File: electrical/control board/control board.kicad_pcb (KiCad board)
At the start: 4 copper layers, 139.7 x 139.7 mm, 63 parts, among them J1 analog_extra, J10 Motor_2, J11 Motor_3, J12 Motor_4, J13 Motor_5, J14 Motor_6, J15 Motor_7, J16 Motor_8, J2 Programming_Header, J3 USB_B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

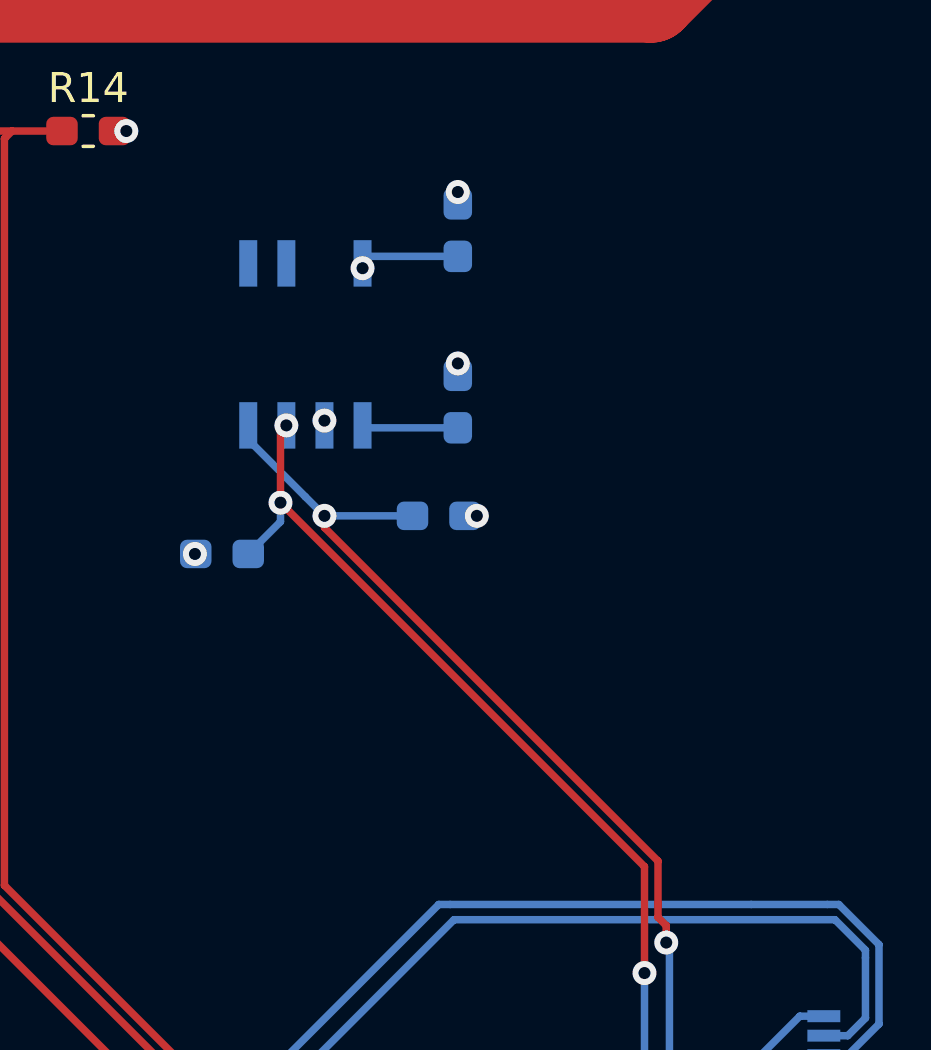
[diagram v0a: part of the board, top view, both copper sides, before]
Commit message: mostly finished routing control board
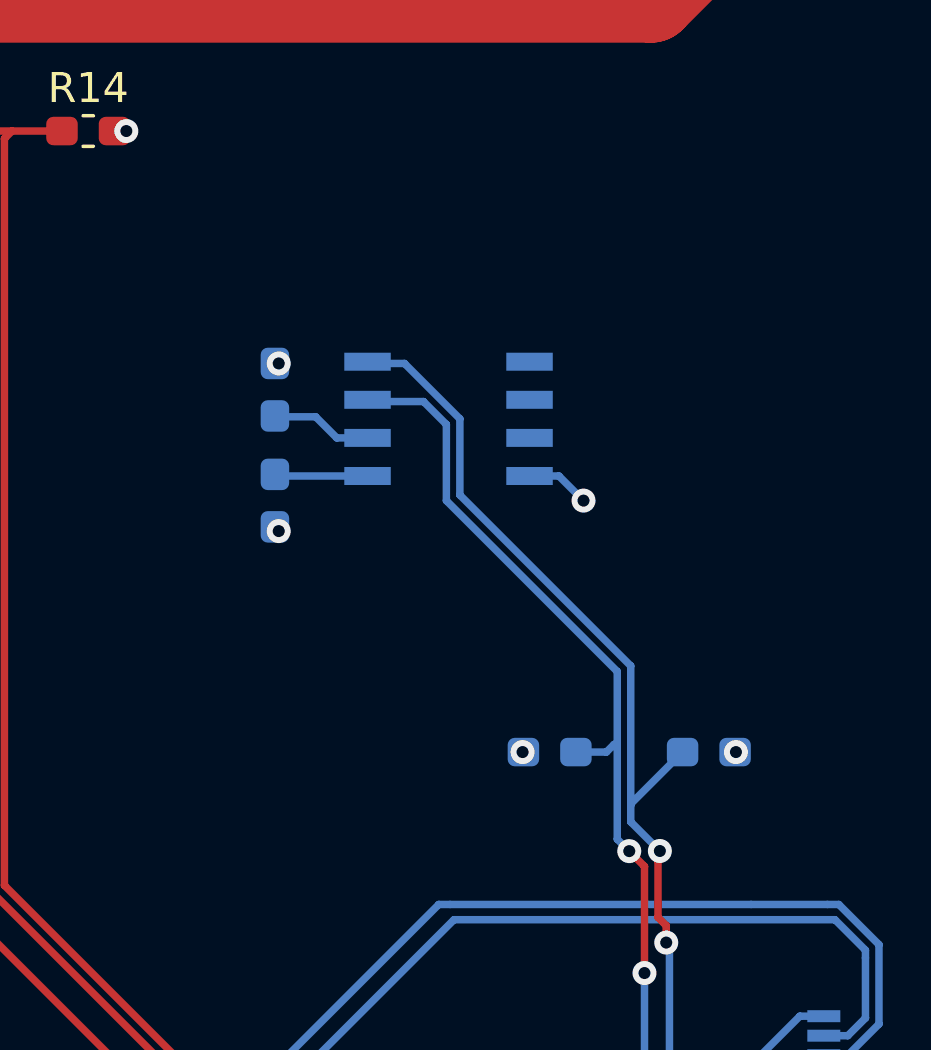
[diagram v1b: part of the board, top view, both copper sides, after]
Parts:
- C1: value 0.1uF -> .22uF
- C4: value 1uF -> .1uF
- R1, R2: value 4.7k -> 2.2k
- U2: value HIH6031 -> HIH6131-021; footprint Package_SO:SOIC-8-N7_3.9x4.9mm_P1.27mm -> Package_SO:SOIC-8_3.9x4.9mm_P1.27mm
- moved R1 12.8 mm to (78.9, 74.7)
- moved R2 12.0 mm to (84.2, 74.7)
- moved C4 10.9 mm to (69.7, 66.3), turned to 270 degrees
- moved C1 6.11 mm to (69.7, 62.6)
- moved U2 5.38 mm to (75.5, 63.6), turned to 0 degrees
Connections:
- C1 pad 2: GND -> +3V3
- C4 pad 1: +3V3 -> Net-(C4-Pad1)
- C4 pad 2: GND -> +3V3
- U2 pad 1: Net-(C1-Pad1) -> Net-(C4-Pad1)
- U2 pad 2: GND -> Net-(C1-Pad1)
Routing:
- net Net-(C4-Pad1): track 0.00 -> 2.98 mm
- net +3V3: track 39.4 -> 38.3 mm, vias 34 -> 36
- net /HIH_SDA: track 62.8 -> 63.5 mm
- net /HIH_SCL: track 60.2 -> 60.0 mm, vias 3 -> 2
- net GND: vias 36 -> 33

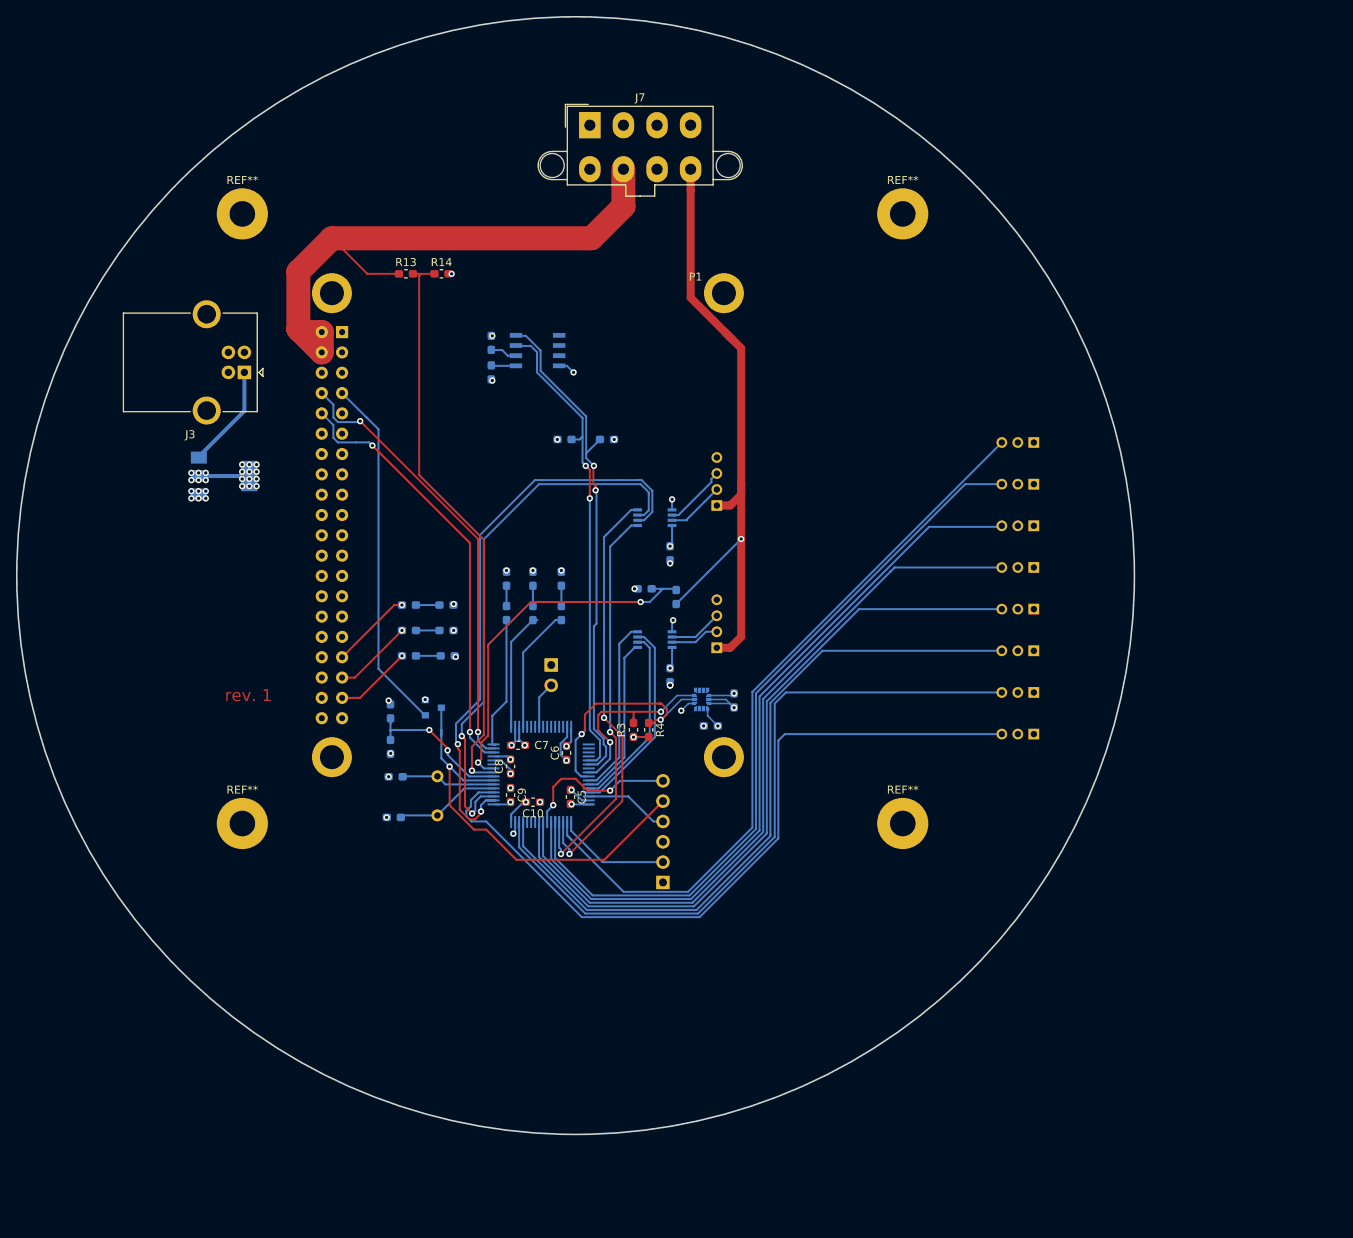
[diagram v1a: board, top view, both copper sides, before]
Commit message: added capacitors to linear regulator
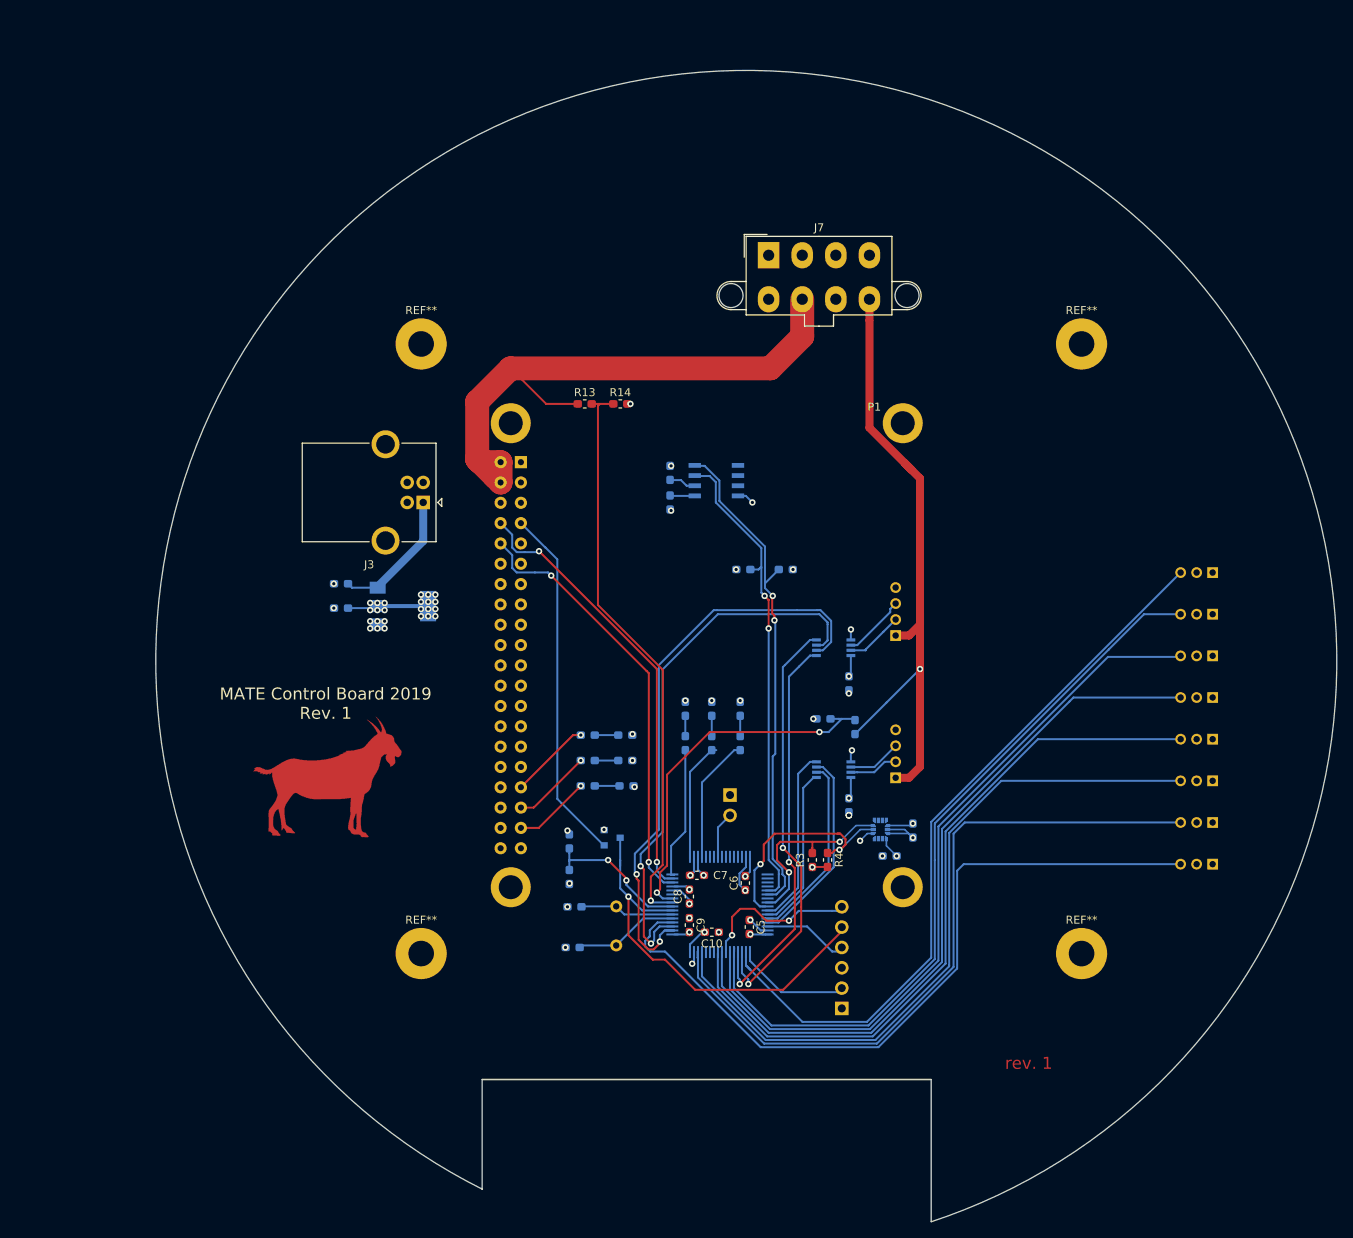
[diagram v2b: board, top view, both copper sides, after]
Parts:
- added C15: 10uF, Capacitor_SMD:C_0603_1608Metric_Pad1.05x0.95mm_HandSolder, B.Cu at (50.9, 92.7)
- added C16: 10uF, Capacitor_SMD:C_0603_1608Metric_Pad1.05x0.95mm_HandSolder, B.Cu at (50.9, 95.8)
- added G***: LOGO, goat:goat_solid_copper_0.731in, F.Cu at (49.3, 116.8)
- moved C8 27.6 mm to (94.5, 131.8)
- moved P1 27.6 mm to (121.2, 72.6)
- moved U2 27.6 mm to (97.9, 79.8)
- moved C11 27.6 mm to (119.5, 126.7)
- moved C12 27.6 mm to (122.4, 123.6)
- moved C13 27.6 mm to (114.4, 120.4)
- moved C14 27.6 mm to (114.4, 105.2)
- moved C3 27.6 mm to (80.1, 133.1)
- moved C4 27.6 mm to (92.1, 82.5)
- moved C9 27.6 mm to (94.5, 135.4)
- moved D1 27.6 mm to (94.0, 108.3)
- moved D4 27.6 mm to (86.5, 111.6)
- moved D5 27.6 mm to (86.5, 114.8)
- moved D6 27.6 mm to (86.6, 118.0)
- moved J1 27.6 mm to (99.6, 119.1)
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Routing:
- net Net-(C15-Pad1): track 13.1 -> 16.8 mm
- net +3V3: track 38.3 -> 41.6 mm
- net GND: vias 33 -> 35
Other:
- board size 139.7 x 139.7 mm -> 147.6 x 143.9 mm
- board text added: "MATE Control Board 2019 Rev. 1"

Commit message: Added pads to access internal layers
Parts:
- added J8: Power_Header, footprints:1x2 individual header, F.Cu at (71.4, 49.8)
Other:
- board text added: "+3.3V"
- board text added: "GND"
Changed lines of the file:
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@@
   (general
     (thickness 1.6)
-    (drawings 6)
+    (drawings 10)
     (tracks 570)
     (zones 0)
-    (modules 66)
+    (modules 67)
     (nets 120)
   )
@@
     )
   )
+  (module "footprints:1x2 individual header" (layer F.Cu)
+    (at 71.374 49.784)
+    (fp_text reference J8 (at 0 0.5) (layer F.SilkS)
+      (effects (font (size 1 1) (thickness 0.15)))
+    )
+    (fp_text value Power_Header (at 0 -0.5) (layer F.Fab)
+      (effects (font (size 1 1) (thickness 0.15)))
+    )
+    (pad 1 thru_hole rect (at -6.35 1.27) (size 1.524 1.524) (drill 0.762) (layers *.Cu *.Mask)
+      (net 1 GND))
+    (pad 2 thru_hole circle (at 6.35 1.27) (size 1.524 1.524) (drill 0.762) (layers *.Cu *.Mask)
+      (net 2 +3V3))
+  )
+  (gr_text +3.3V (at 77.724 48.514) (layer B.SilkS)
+    (effects (font (size 1.5 1.5) (thickness 0.3)) (justify mirror))
+  )
+  (gr_text GND (at 64.77 48.514) (layer B.SilkS)
+    (effects (font (size 1.5 1.5) (thickness 0.3)) (justify mirror))
+  )
+  (gr_text +3.3V (at 77.216 53.594) (layer F.SilkS)
+    (effects (font (size 1.5 1.5) (thickness 0.3)))
+  )
+  (gr_text GND (at 64.77 53.594) (layer F.SilkS)
+    (effects (font (size 1.5 1.5) (thickness 0.3)))
+  )
   (gr_text "MATE Control Board 2019\nRev. 1" (at 49.022 107.696) (layer F.SilkS)

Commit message: Marked diode polarity
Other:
- board text added: "-"
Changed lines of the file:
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@@
   (general
     (thickness 1.6)
-    (drawings 10)
+    (drawings 16)
     (tracks 570)
     (zones 0)
@@
       (net 2 +3V3))
   )
+  (gr_text - (at 100.838 105.664) (layer B.SilkS)
+    (effects (font (size 1.5 1.5) (thickness 0.3)) (justify mirror))
+  )
+  (gr_text - (at 97.282 105.664) (layer B.SilkS)
+    (effects (font (size 1.5 1.5) (thickness 0.3)) (justify mirror))
+  )
+  (gr_text - (at 93.98 105.664) (layer B.SilkS)
+    (effects (font (size 1.5 1.5) (thickness 0.3)) (justify mirror))
+  )
+  (gr_text - (at 89.154 111.506) (layer B.SilkS)
+    (effects (font (size 1.5 1.5) (thickness 0.3)) (justify mirror))
+  )
+  (gr_text - (at 89.154 114.554) (layer B.SilkS)
+    (effects (font (size 1.5 1.5) (thickness 0.3)) (justify mirror))
+  )
+  (gr_text - (at 89.154 117.856) (layer B.SilkS)
+    (effects (font (size 1.5 1.5) (thickness 0.3)) (justify mirror))
+  )
   (gr_text +3.3V (at 77.724 48.514) (layer B.SilkS)

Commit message: added reset button
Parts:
- added C17: .1uF, Capacitor_SMD:C_0603_1608Metric_Pad1.05x0.95mm_HandSolder, F.Cu at (97.4, 133.3)
- added C18: 2.2uF, Capacitor_SMD:C_0603_1608Metric_Pad1.05x0.95mm_HandSolder, B.Cu at (102.9, 122.5)
- added SW1: SW_Push, Button_Switch_SMD:SW_SPST_PTS645, B.Cu at (87.9, 145.8)
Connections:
- U1 pad 60: Net-(U1-Pad60) -> GND
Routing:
- net /NRST: track 52.3 -> 67.8 mm, vias 1 -> 4
- net GND: track 24.5 -> 31.2 mm, vias 35 -> 38
- net Net-(C18-Pad1): track 0.00 -> 4.41 mm

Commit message: connected stuff
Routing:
- net GND: track 31.2 -> 34.2 mm, vias 38 -> 39
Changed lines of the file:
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@@
     (thickness 1.6)
     (drawings 16)
-    (tracks 589)
+    (tracks 593)
     (zones 0)
     (modules 70)
@@
     (effects (font (size 1.5 1.5) (thickness 0.3)))
   )
+  (via (at 102.87 121.666) (size 0.8) (drill 0.4) (layers F.Cu B.Cu) (net 1))
   (via (at 98.298 133.35) (size 0.8) (drill 0.4) (layers F.Cu B.Cu) (net 1))
   (via (at 50.038 95.758) (size 0.8) (drill 0.4) (layers F.Cu B.Cu) (net 1))
@@
   (via (at 55.488 98.298) (size 0.8) (drill 0.4) (layers F.Cu B.Cu) (net 1))
   (via (at 54.588 98.298) (size 0.8) (drill 0.4) (layers F.Cu B.Cu) (net 1))
-  (via (at 98.171 136.271) (size 0.8) (drill 0.4) (layers F.Cu B.Cu) (net 1))
   (via (at 94.488 134.493) (size 0.8) (drill 0.4) (layers F.Cu B.Cu) (net 1))
   (via (at 87.63 118.11) (size 0.8) (drill 0.4) (layers F.Cu B.Cu) (net 1))
@@
   (segment (start 91.864 148.046) (end 92.928 148.046) (width 0.25) (layer B.Cu) (net 1))
   (segment (start 92.928 148.046) (end 94.234 149.352) (width 0.25) (layer B.Cu) (net 1))
+  (via (at 98.298 136.398) (size 0.8) (drill 0.4) (layers F.Cu B.Cu) (net 1))
+  (segment (start 97.954049 136.398) (end 98.298 136.398) (width 0.25) (layer B.Cu) (net 1))
+  (segment (start 96.560109 138.501942) (end 96.560109 137.79194) (width 0.25) (layer B.Cu) (net 1))
+  (segment (start 96.560109 137.79194) (end 97.954049 136.398) (width 0.25) (layer B.Cu) (net 1))
   (via (at 56.388 96.012) (size 0.8) (drill 0.4) (layers F.Cu B.Cu) (net 2))
   (via (at 62.738 96.774) (size 0.8) (drill 0.4) (layers F.Cu B.Cu) (net 2))

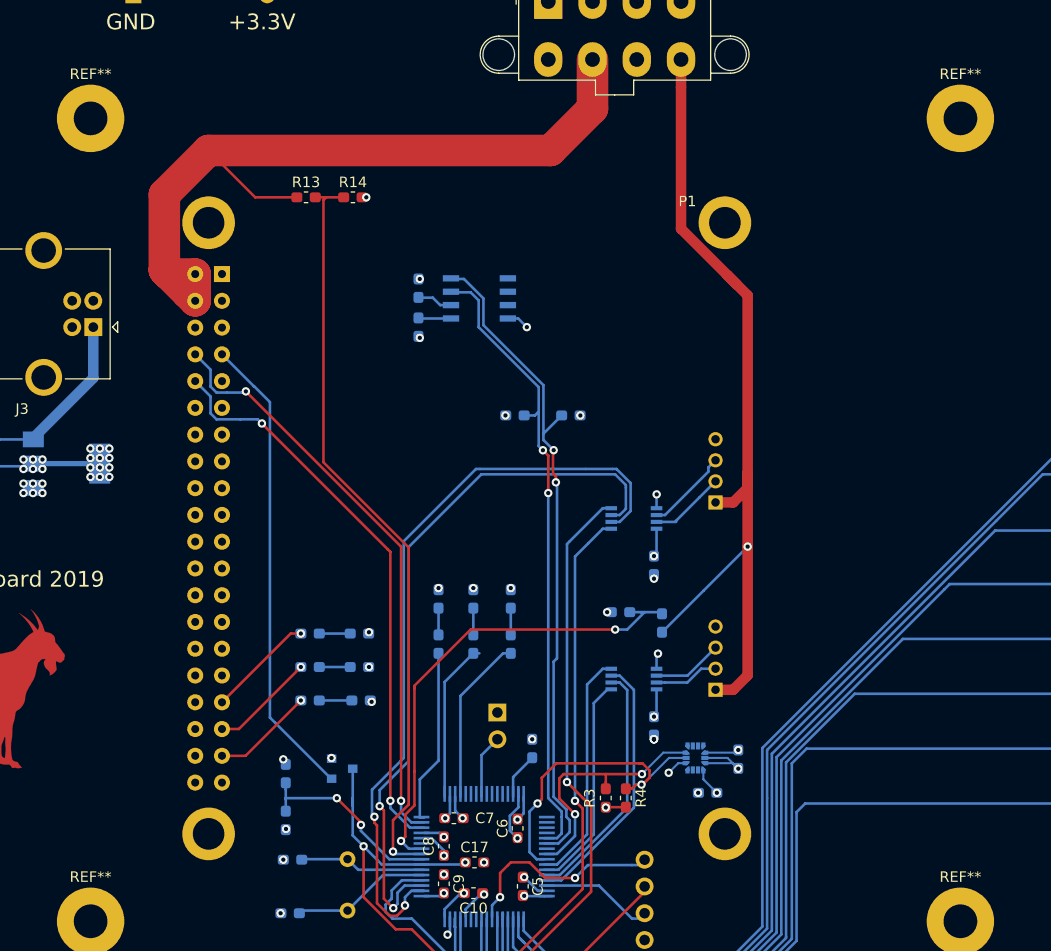
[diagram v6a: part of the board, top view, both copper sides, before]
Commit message: Added low side switch connector
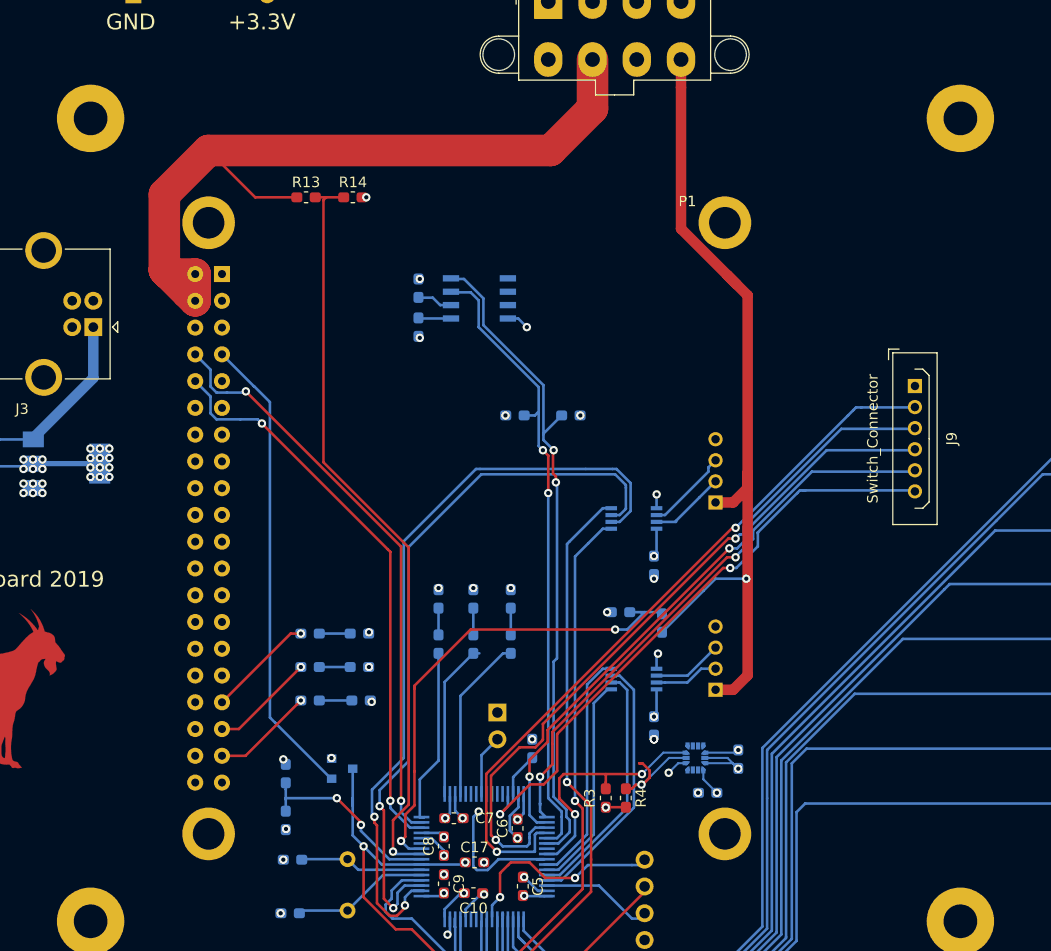
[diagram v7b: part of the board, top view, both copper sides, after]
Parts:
- added J9: Switch_Connector, Connector_Harwin:Harwin_LTek-Male_06_P2.00mm_Vertical, F.Cu at (139.2, 88.1)
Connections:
- U1 pad 26: /SWITCH_A -> Net-(U1-Pad26)
- U1 pad 27: /SWITCH_B -> Net-(U1-Pad27)
- U1 pad 29: Net-(U1-Pad29) -> /SWITCH_A
- U1 pad 33: Net-(U1-Pad33) -> /SWITCH_B
- U1 pad 34: Net-(U1-Pad34) -> /SWITCH_C
- U1 pad 35: Net-(U1-Pad35) -> /SWITCH_D
- U1 pad 36: Net-(U1-Pad36) -> /SWITCH_E
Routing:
- net /SWITCH_E: track 0.00 -> 69.1 mm, vias 0 -> 2
- net /SWITCH_D: track 0.00 -> 67.5 mm, vias 0 -> 2
- net /SWITCH_A: track 0.00 -> 57.0 mm, vias 0 -> 2
- net /SWITCH_C: track 0.00 -> 56.8 mm, vias 0 -> 2
- net /SWITCH_B: track 0.00 -> 54.4 mm, vias 0 -> 2
- net /ICM_SCL: track 29.2 -> 23.6 mm
- net +48V: track 82.7 -> 81.3 mm
